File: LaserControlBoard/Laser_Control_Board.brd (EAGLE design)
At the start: 50.8 x 50.8 mm, 28 parts, among them J1 Servo Header, J2 FTDI Header, U1 ATMEGA328P_TQFP, Y1 16MHz

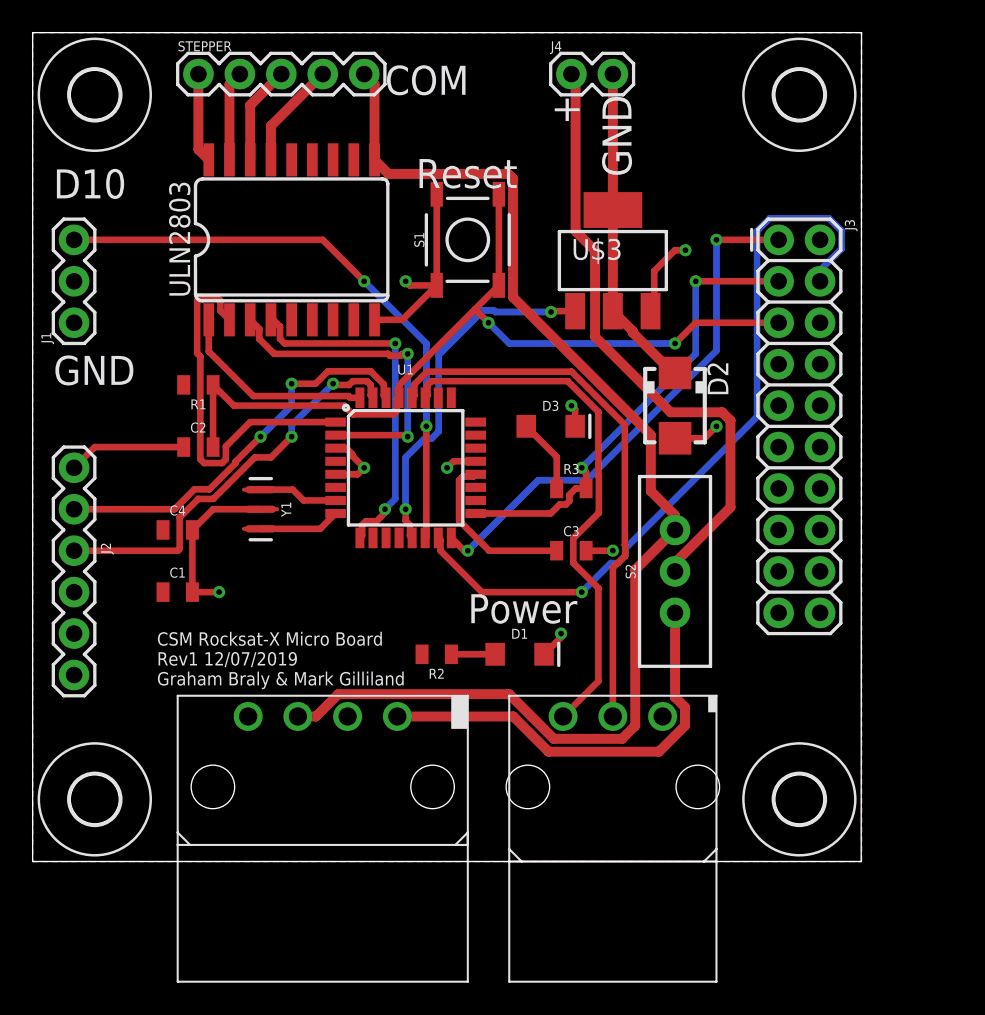
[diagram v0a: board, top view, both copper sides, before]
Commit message: Added second MOSFET to subsystem control board and rerouted.
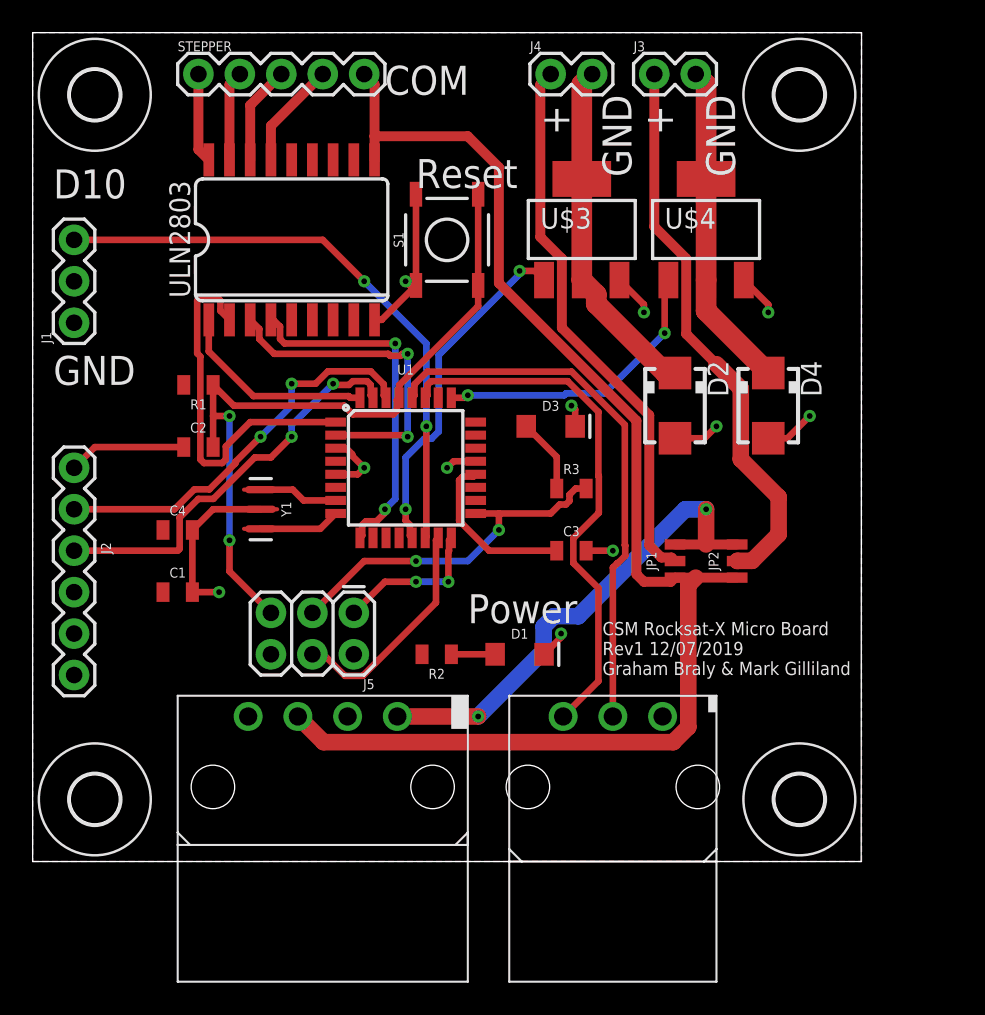
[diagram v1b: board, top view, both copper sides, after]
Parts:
- removed S2: (no value), SparkFun-Switches:SWITCH_SPDT_PTH_11.6X4.0MM
- added D4: S1M, diode:SMA
- added J5: FEMALE 2x3, SparkFun-Connectors:2X3
- added JP1, JP2: (no value), SparkFun-Jumpers:SMT-JUMPER_3_0-NO_TRACE_NO-SILK
- added U$4: BUK9880-55A, PowerManagementParts:SOT223
- J3: device SparkFun-Connectors:2X10 -> SparkFun-Connectors:1X02
- moved J3 12.7 mm to (38.1, 48.3), turned to 0 degrees
- moved U$3 2.69 mm to (33.7, 38.7)
- moved J4 1.27 mm to (31.8, 48.3)
- moved S1 1.27 mm to (25.4, 38.1)
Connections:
- net MOSFET_SWITCHED renamed MOSFET_SWITCHED_1
- new net MOSFET_SWITCHED_2: D4.C, J3.2, U$4.2, U$4.4
- new net N$8: J3.1, JP2.2
- new net PB0: U1.12
- new net PC0: U1.23
- new net PC1: U1.24
- new net PC2: U$4.1, U1.25
- new net PC3: U1.26
- new net PD6: U1.10
- new net PD7: U1.11
- net 12V: now also JP1.3, JP2.3; no longer S2.3
- net 5V_ACT: now also JP1.1, JP2.1; no longer S2.1
- net GND: now also D4.A, J5.6, U$4.3; no longer J3.6
- net MISO: now also J5.1; no longer J3.1
- net MOSI: now also J5.4; no longer J3.4
- net N$1: now also JP1.2; no longer S2.2
- net RESET: now also J5.5; no longer J3.5
- net SCK: now also J5.3; no longer J3.3
- net VCC: now also J5.2; no longer J3.2
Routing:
- net N$8: track 0.00 -> 34.6 mm
- net MOSI: track 46.9 -> 14.0 mm, vias 1 -> 0
- net MISO: track 32.3 -> 9.35 mm
- net MOSFET_SWITCHED_2: track 0.00 -> 20.2 mm
- net PC2: track 0.00 -> 18.1 mm, vias 0 -> 2
- net 5V_ACT: track 75.8 -> 83.1 mm
- net RESET: track 51.8 -> 45.4 mm
- net SCK: track 28.4 -> 22.2 mm
- net 12V: track 26.4 -> 31.0 mm, vias 0 -> 2
- net N$1: track 37.8 -> 33.9 mm
- net MOSFET_SWITCHED_1: track 20.0 -> 21.3 mm
- net GND: track 41.1 -> 41.9 mm, vias 9 -> 11
- net PB1: track 22.0 -> 21.4 mm

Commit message: Breakout headers added to Experiment Control board.
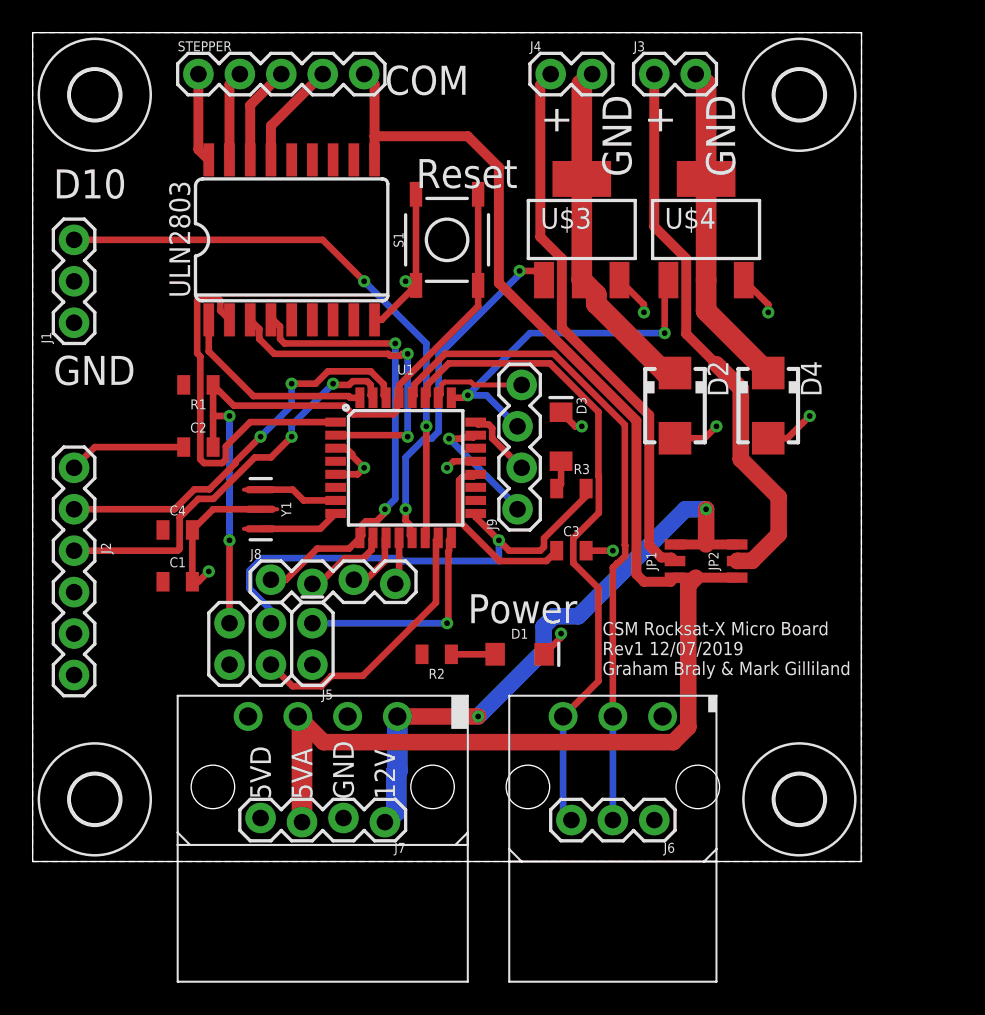
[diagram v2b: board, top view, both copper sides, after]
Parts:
- added J6: 455-1750-1-ND, SparkFun-Connectors:1X03
- added J7, J8, J9: (no value), SparkFun-Connectors:1X04_LOCK
- moved J5 2.62 mm to (17.1, 14.6)
- moved D3 0.90 mm to (32.4, 26.0), turned to 90 degrees
- moved C1 0.63 mm to (8.89, 17.1)
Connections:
- net 12V: now also J7.1
- net 5V_ACT: now also J7.3
- net GND: now also J6.1, J7.2
- net PB0: now also J8.4
- net PC0: now also J9.1
- net PC1: now also J9.2
- net PC2: now also J9.3
- net PC3: now also J9.4
- net PD5: now also J8.1
- net PD6: now also J8.2
- net PD7: now also J8.3
- net SCL: now also J6.2
- net SDA: now also J6.3
- net VCC: now also J7.4
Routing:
- net SCK: track 22.2 -> 30.7 mm, vias 2 -> 1
- net PC0: track 0.00 -> 7.78 mm, vias 0 -> 1
- net SDA: track 33.1 -> 40.5 mm
- net SCL: track 33.7 -> 40.9 mm
- net 12V: track 31.0 -> 37.8 mm
- net 5V_ACT: track 83.1 -> 89.7 mm
- net PD5: track 21.9 -> 28.4 mm
- net PC3: track 0.00 -> 5.93 mm
- net PD6: track 0.00 -> 5.27 mm
- net PC1: track 0.00 -> 4.35 mm
- net MISO: track 9.35 -> 13.6 mm, vias 2 -> 1
- net PC2: track 18.1 -> 21.9 mm
- net PD7: track 0.00 -> 3.83 mm
- net PB0: track 0.00 -> 2.92 mm
- net MOSI: track 14.0 -> 16.8 mm
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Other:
- board text added: "12V"
- board text added: "5VA"
- board text added: "5VD"
